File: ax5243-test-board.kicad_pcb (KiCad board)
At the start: 2 copper layers, 43.2 x 18 mm, 39 parts, among them J1 Conn_Coaxial, J2 Conn_01x15, J3 Conn_01x15, U1 AX5243, X1 12MHz

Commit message: Add part numbers and Digikey SKUs
Also change TCXO frequency to 26 MHz.
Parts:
- C14: value DNP -> 100nF
- C15: value DNP -> 1nF
- C16: value 6.8pF -> DNP
- C17: value 10pF -> 1nF
- J1: value Conn_Coaxial -> CONSMA008-G
- R2: value DNP -> 100
- R3: value DNP -> 1k
- X1: value 12MHz -> 26MHz

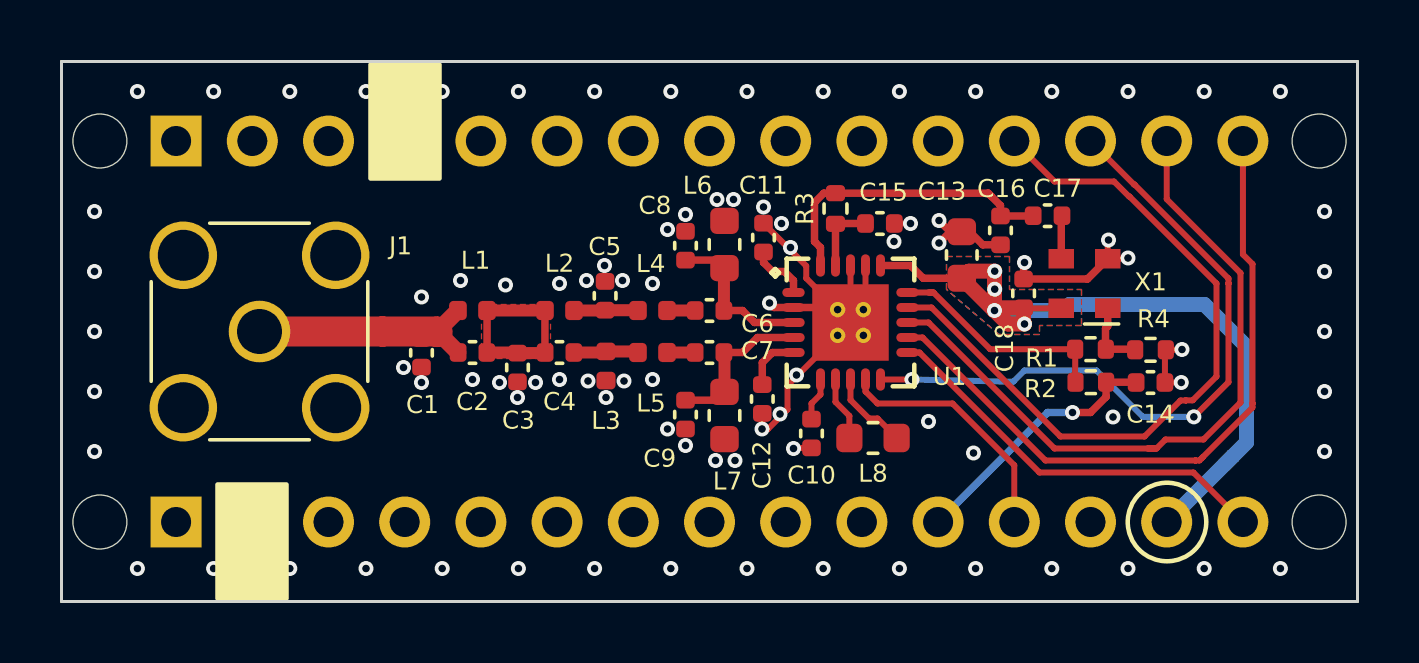
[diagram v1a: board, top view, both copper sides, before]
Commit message: Move the extension connections to the correct location
Add solder mask extension.
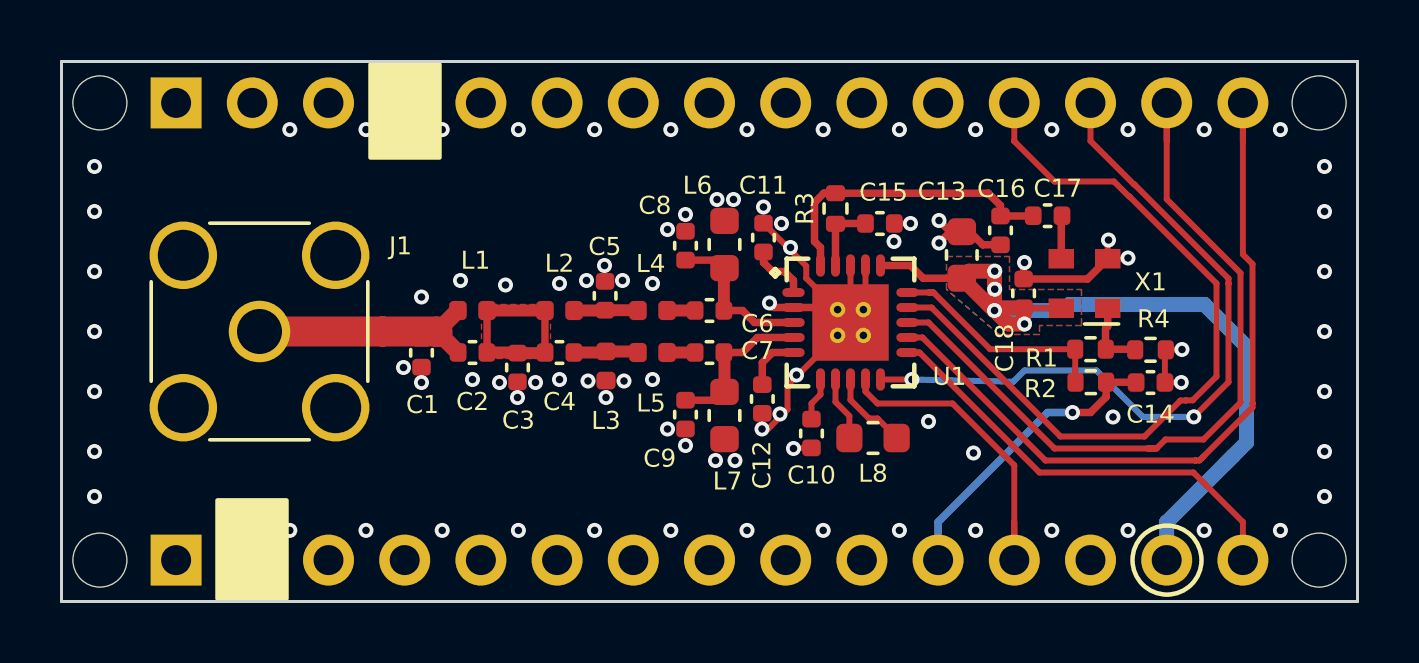
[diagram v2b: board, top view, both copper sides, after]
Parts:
- moved H1 1.27 mm to (123.7, 74.4)
- moved H2 1.27 mm to (164.3, 74.4)
- moved H3 1.27 mm to (123.7, 89.6)
- moved H4 1.27 mm to (164.3, 89.6)
- moved J2 1.27 mm to (126.2, 74.4)
- moved J3 1.27 mm to (126.2, 89.6)
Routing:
- net SYSCLK: track 8.07 -> 10.6 mm
- net MOSI: track 23.5 -> 26.0 mm
- net MISO: track 22.9 -> 25.5 mm
- net IRQ: track 24.7 -> 26.0 mm
- net CLK: track 13.5 -> 14.8 mm
- net VDD: track 27.8 -> 29.1 mm
- net SEL: track 22.8 -> 24.1 mm
- net DAC_OUT: track 8.91 -> 10.1 mm
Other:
- board text added: "AX5243 SHIELD ARDUINO NANO 3.3V FEB 2021 REV B"
- board text removed: "AX5243 SHIELD ARDUINO NANO 3.3V JAN 2021"

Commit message: New kicad nigtly version
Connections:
- J2 pad 1: no_connect_28 -> unconnected-(J2-Pad1)
- J2 pad 10: no_connect_29 -> unconnected-(J2-Pad10)
- J2 pad 11: no_connect_30 -> unconnected-(J2-Pad11)
- J2 pad 2: no_connect_31 -> unconnected-(J2-Pad2)
- J2 pad 3: no_connect_32 -> unconnected-(J2-Pad3)
- J2 pad 5: no_connect_33 -> unconnected-(J2-Pad5)
- J2 pad 6: no_connect_34 -> unconnected-(J2-Pad6)
- J2 pad 7: no_connect_35 -> unconnected-(J2-Pad7)
- J2 pad 8: no_connect_36 -> unconnected-(J2-Pad8)
- J2 pad 9: no_connect_37 -> unconnected-(J2-Pad9)
- J3 pad 1: no_connect_38 -> unconnected-(J3-Pad1)
- J3 pad 10: no_connect_39 -> unconnected-(J3-Pad10)
- J3 pad 13: no_connect_40 -> unconnected-(J3-Pad13)
- J3 pad 3: no_connect_41 -> unconnected-(J3-Pad3)
- J3 pad 4: no_connect_42 -> unconnected-(J3-Pad4)
- J3 pad 5: no_connect_43 -> unconnected-(J3-Pad5)
- J3 pad 6: no_connect_44 -> unconnected-(J3-Pad6)
- J3 pad 7: no_connect_45 -> unconnected-(J3-Pad7)
- J3 pad 8: no_connect_46 -> unconnected-(J3-Pad8)
- J3 pad 9: no_connect_47 -> unconnected-(J3-Pad9)
